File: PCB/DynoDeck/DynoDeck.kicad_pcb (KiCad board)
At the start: 4 copper layers, 105 x 107.3 mm, 76 parts, among them J1 USB_C_Receptacle_USB2.0_16P, J2 PGRM, J3 CardKBConn, J4 E-paper, J5 HC-IPEX0125-01 (u.FL), J6 BWSMA-KWE-Z001 (SMA), J7 CardKBRef, SW1 QON, SW2 POWER, SW3 RESET, SW4 IO1, U1 BQ25895RTW, U2 USBLC6-2SC6, U3 SX1262IMLTRT, U4 TUSB320, U5 MD7218E33PC1, U6 E73-2G4M08S1C, U7 PE42422MLAA-Z, U8 PE42422MLAA-Z, Y1 OW7EL89CENUXK7YLC-32M, Y3 3N00032G33YC

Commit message: nRF wiring finish I think
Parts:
- moved J6 0.60 mm to (126.9, 32.7)
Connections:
- U6 pad 10: /OTG -> /~{CE}
- U6 pad 28: unconnected-(U6B-P0.15-Pad28) -> /SDA
- U6 pad 30: unconnected-(U6B-P0.17-Pad30) -> /SCL
- U6 pad 9: /~{CE} -> /OTG
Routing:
- net /SCL: track 0.00 -> 161.5 mm, vias 0 -> 4
- net /SDA: track 0.00 -> 152.4 mm, vias 0 -> 6
- net /~{INT}: track 3.74 -> 97.8 mm, vias 0 -> 6
- net /OTG: track 5.46 -> 97.6 mm, vias 0 -> 6
- net /~{CE}: track 28.4 -> 99.0 mm, vias 4 -> 6
- net unconnected-(U6B-P0.17-Pad30): track 11.7 -> 0.00 mm, vias 2 -> 0
- net unconnected-(U6B-P0.15-Pad28): track 11.1 -> 0.00 mm, vias 2 -> 0
- added copper zone on F.Cu, net GND

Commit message: pcb done?
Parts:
- moved L3 1.78 mm to (120.8, 56.2)
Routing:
- net +3V3: track 29.1 -> 38.5 mm, vias 14 -> 27
- net Net-(U3-VREG): track 11.2 -> 12.2 mm
- net GND: track 18.2 -> 19.0 mm, vias 19 -> 1031

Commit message: Fix DRC errors
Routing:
- net +3V3: track 38.5 -> 42.1 mm, vias 27 -> 30
- net GND: track 19.0 -> 20.1 mm, vias 1031 -> 1044

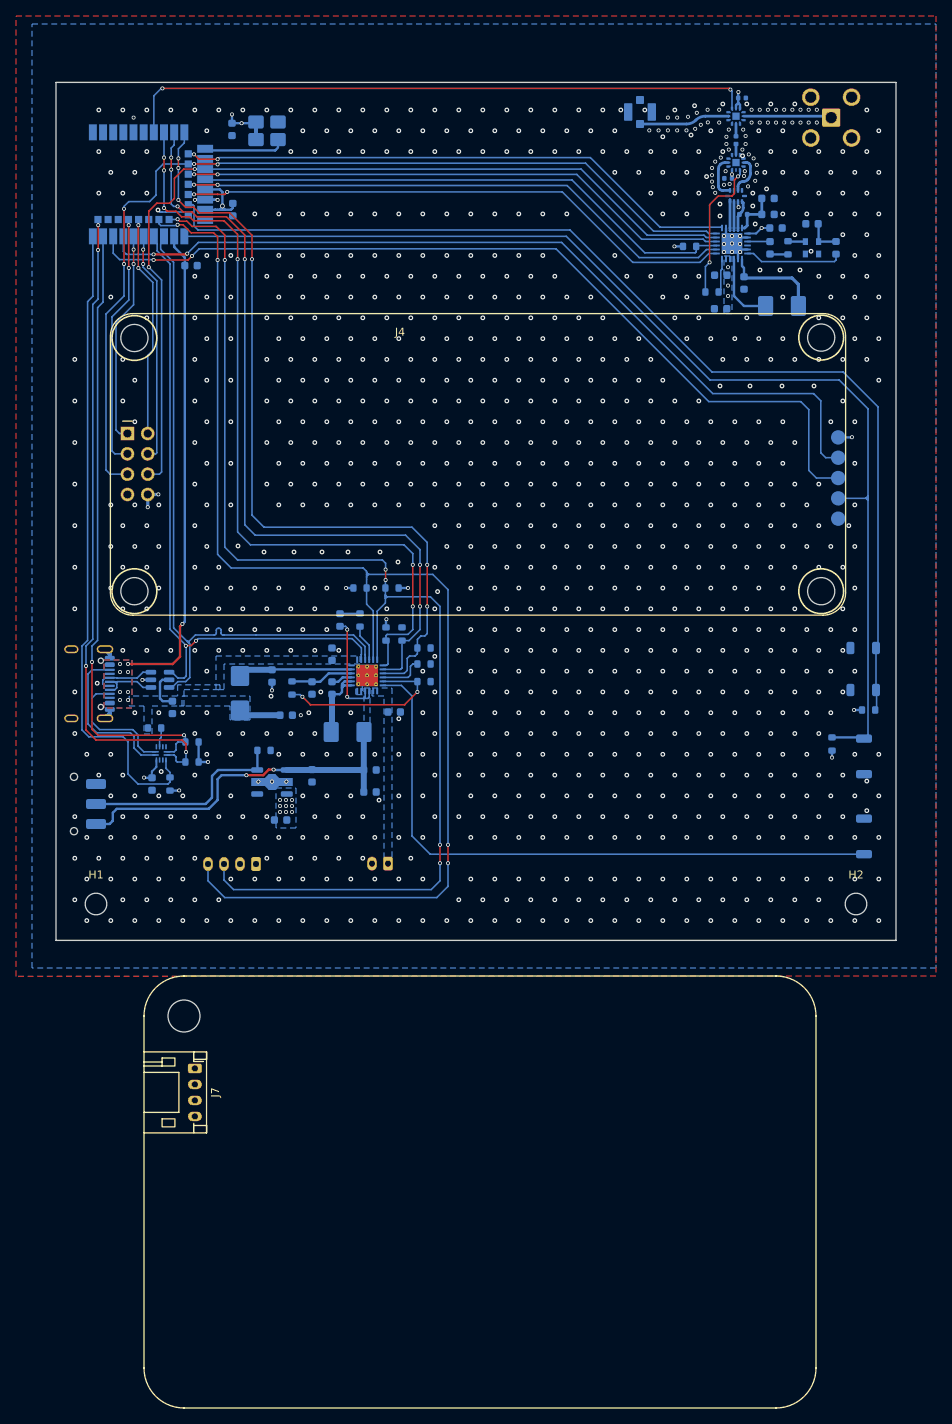
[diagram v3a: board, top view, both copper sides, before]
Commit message: Update mounting hole + DRC stuff
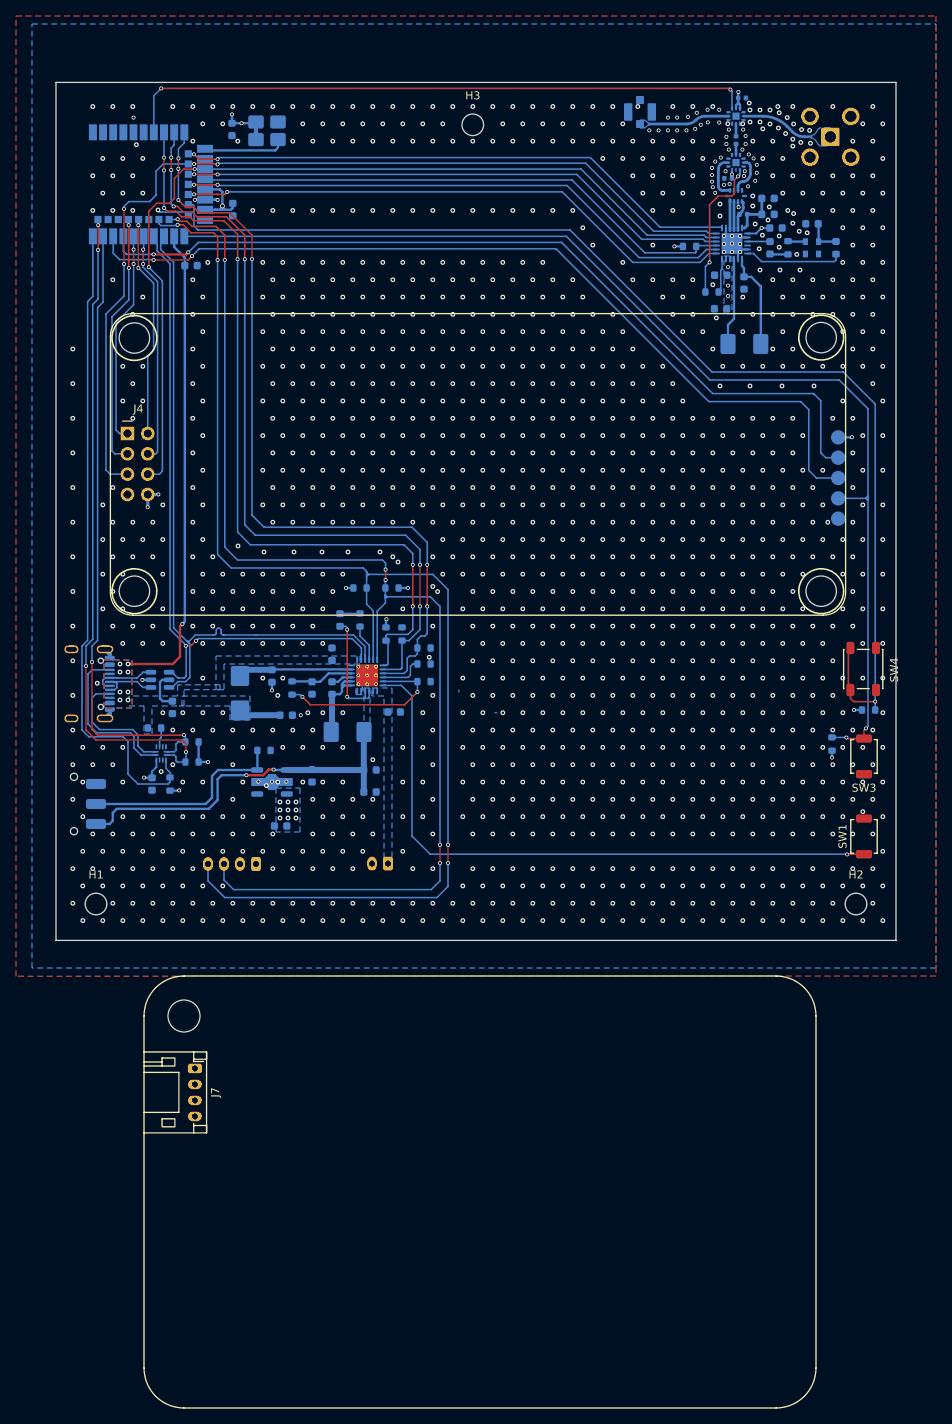
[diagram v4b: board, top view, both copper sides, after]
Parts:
- added H3: MountingHole, MountingHole:MountingHole_2.7mm_M2.5, F.Cu at (82.1, 33.6)
- SW1, SW3, SW4: moved to F.Cu
- moved L3 6.68 mm to (116.0, 61.0)
- moved J6 2.40 mm to (126.8, 35.1)
- moved C19 0.75 mm to (58.1, 121.2)
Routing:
- net /USER1: track 136.4 -> 145.7 mm, vias 0 -> 1
- net /ANT2: track 11.3 -> 9.23 mm
- net Net-(U3-DCC_SW): track 9.09 -> 10.9 mm
- net /ANT1: track 11.4 -> 10.2 mm
- net /nRESET: track 144.4 -> 144.5 mm, vias 0 -> 2
- net Net-(U1-~{QON}): vias 0 -> 1
- net GND: vias 1044 -> 1441
- added copper zone on B.Cu, net /ANT1
- added copper zone on B.Cu, net /ANT2
